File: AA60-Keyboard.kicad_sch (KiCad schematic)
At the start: 0 parts

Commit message: MCU/USB/Switch Matrix Schematics
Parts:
- added C1: 4.7uF, symbol Device:C
- added C2, C4, C5: 0.1uF, symbol Device:C
- added C3, C6, C7: 1uF, symbol Device:C
- added F1: 1A, symbol Device:Polyfuse
- added J2: USB_C_Receptacle_USB2.0_16P, symbol Connector:USB_C_Receptacle_USB2.0_16P
- added R1: 10k, symbol Device:R
- added R2, R3: 5.1k, symbol Device:R
- added SW1: SW_Push, symbol Switch:SW_Push
- added SW2: SW_SPDT, symbol Switch:SW_SPDT
- added U1: STM32G0B1CBTx, Package_QFP:LQFP-48_7x7mm_P0.5mm, symbol MCU_ST_STM32G0:STM32G0B1CBTx
- added U2: SRV05-4, Package_TO_SOT_SMD:SOT-23-6, symbol Power_Protection:SRV05-4
- added U3: XC6206P332MR, Package_TO_SOT_SMD:SOT-23-3, symbol Regulator_Linear:XC6206PxxxMR
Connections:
- new net: J2.B5 (CC2), R3.1
- new net: J2.A5 (CC1), R2.2
- new net: R1.1, SW2.2 (B)
- new net +3.3V: C1.1, C2.1, C3.1, C4.1, C7.1, SW2.3 (C), U1.4 (VBAT), U1.5 (VREF+), U1.6 (VDD), U3.2 (VO)
- new net +5V: C6.1, F1.2, U2.5 (VP), U3.3 (VI)
- new net BOOT0: R1.2, U1.36 (PA14)
- new net GND: C1.2, C2.2, C3.2, C4.2, C5.2, C6.2, C7.2, J2.A1 (GND), J2.A12 (GND), J2.B1 (GND), J2.B12 (GND), J2.S1 (SHIELD), R2.1, R3.2, SW1.2, SW2.1 (A), U1.7 (VSS), U2.2 (VN), U3.1 (GND)
- new net USB_DM: J2.A7 (D-), J2.B7 (D-), U1.33 (PA9/PA11)
- new net USB_DP: J2.A6 (D+), J2.B6 (D+), U1.34 (PA10/PA12)
- new net VBUS: F1.1, J2.A4 (VBUS), J2.A9 (VBUS), J2.B4 (VBUS), J2.B9 (VBUS)
- new net nRST: C5.1, SW1.1, U1.10 (PF2)
- no-connect marks 0 -> 2
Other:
- added sheet Switch Matrix (matrix.kicad_sch)

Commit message: Footprints
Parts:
- C1, C2, C3, C4, C5, C6, C7: footprint (none) -> Capacitor_SMD:C_0805_2012Metric
- F1: footprint (none) -> Fuse:Fuse_1206_3216Metric
- J2: footprint (none) -> Connector_USB:USB_C_Receptacle_HRO_TYPE-C-31-M-12
- R1, R2, R3: footprint (none) -> Resistor_SMD:R_0805_2012Metric
- SW1: footprint (none) -> Button_Switch_SMD:SW_SPST_TS-1088-xR020
- SW2: footprint (none) -> Button_Switch_SMD:SW_SPDT_PCM12
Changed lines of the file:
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@@
 			)
 		)
-		(property "Footprint" ""
+		(property "Footprint" "Capacitor_SMD:C_0805_2012Metric"
 			(at 139.3952 101.6 0)
 			(effects
@@
 			)
 		)
-		(property "Footprint" ""
+		(property "Footprint" "Resistor_SMD:R_0805_2012Metric"
 			(at 158.242 132.08 90)
 			(effects
@@
 			)
 		)
-		(property "Footprint" ""
+		(property "Footprint" "Resistor_SMD:R_0805_2012Metric"
 			(at 171.958 132.08 90)
 			(effects
@@
 			)
 		)
-		(property "Footprint" ""
+		(property "Footprint" "Capacitor_SMD:C_0805_2012Metric"
 			(at 36.5252 33.02 0)
 			(effects
@@
 			)
 		)
-		(property "Footprint" ""
+		(property "Footprint" "Capacitor_SMD:C_0805_2012Metric"
 			(at 110.1852 101.6 0)
 			(effects
@@
 			)
 		)
-		(property "Footprint" ""
+		(property "Footprint" "Capacitor_SMD:C_0805_2012Metric"
 			(at 23.8252 33.02 0)
 			(effects
@@
 			)
 		)
-		(property "Footprint" ""
+		(property "Footprint" "Capacitor_SMD:C_0805_2012Metric"
 			(at 23.8252 60.96 0)
 			(effects
@@
 			)
 		)
-		(property "Footprint" ""
+		(property "Footprint" "Resistor_SMD:R_0805_2012Metric"
 			(at 72.39 57.658 90)
 			(effects
@@
 			)
 		)
-		(property "Footprint" ""
+		(property "Footprint" "Button_Switch_SMD:SW_SPST_TS-1088-xR020"
 			(at 72.39 27.94 0)
 			(effects
@@
 			)
 		)
-		(property "Footprint" ""
+		(property "Footprint" "Connector_USB:USB_C_Receptacle_HRO_TYPE-C-31-M-12"
 			(at 120.65 135.89 0)
 			(effects
@@
 			)
 		)
-		(property "Footprint" ""
+		(property "Footprint" "Fuse:Fuse_1206_3216Metric"
 			(at 158.75 119.38 0)
 			(effects
@@
 			)
 		)
-		(property "Footprint" ""
+		(property "Footprint" "Button_Switch_SMD:SW_SPDT_PCM12"
 			(at 63.5 55.88 0)
 			(effects
@@
 			)
 		)
-		(property "Footprint" ""
+		(property "Footprint" "Capacitor_SMD:C_0805_2012Metric"
 			(at 36.5252 60.96 0)
 			(effects
@@
 			)
 		)
-		(property "Footprint" ""
+		(property "Footprint" "Capacitor_SMD:C_0805_2012Metric"
 			(at 56.8452 30.48 0)
 			(effects

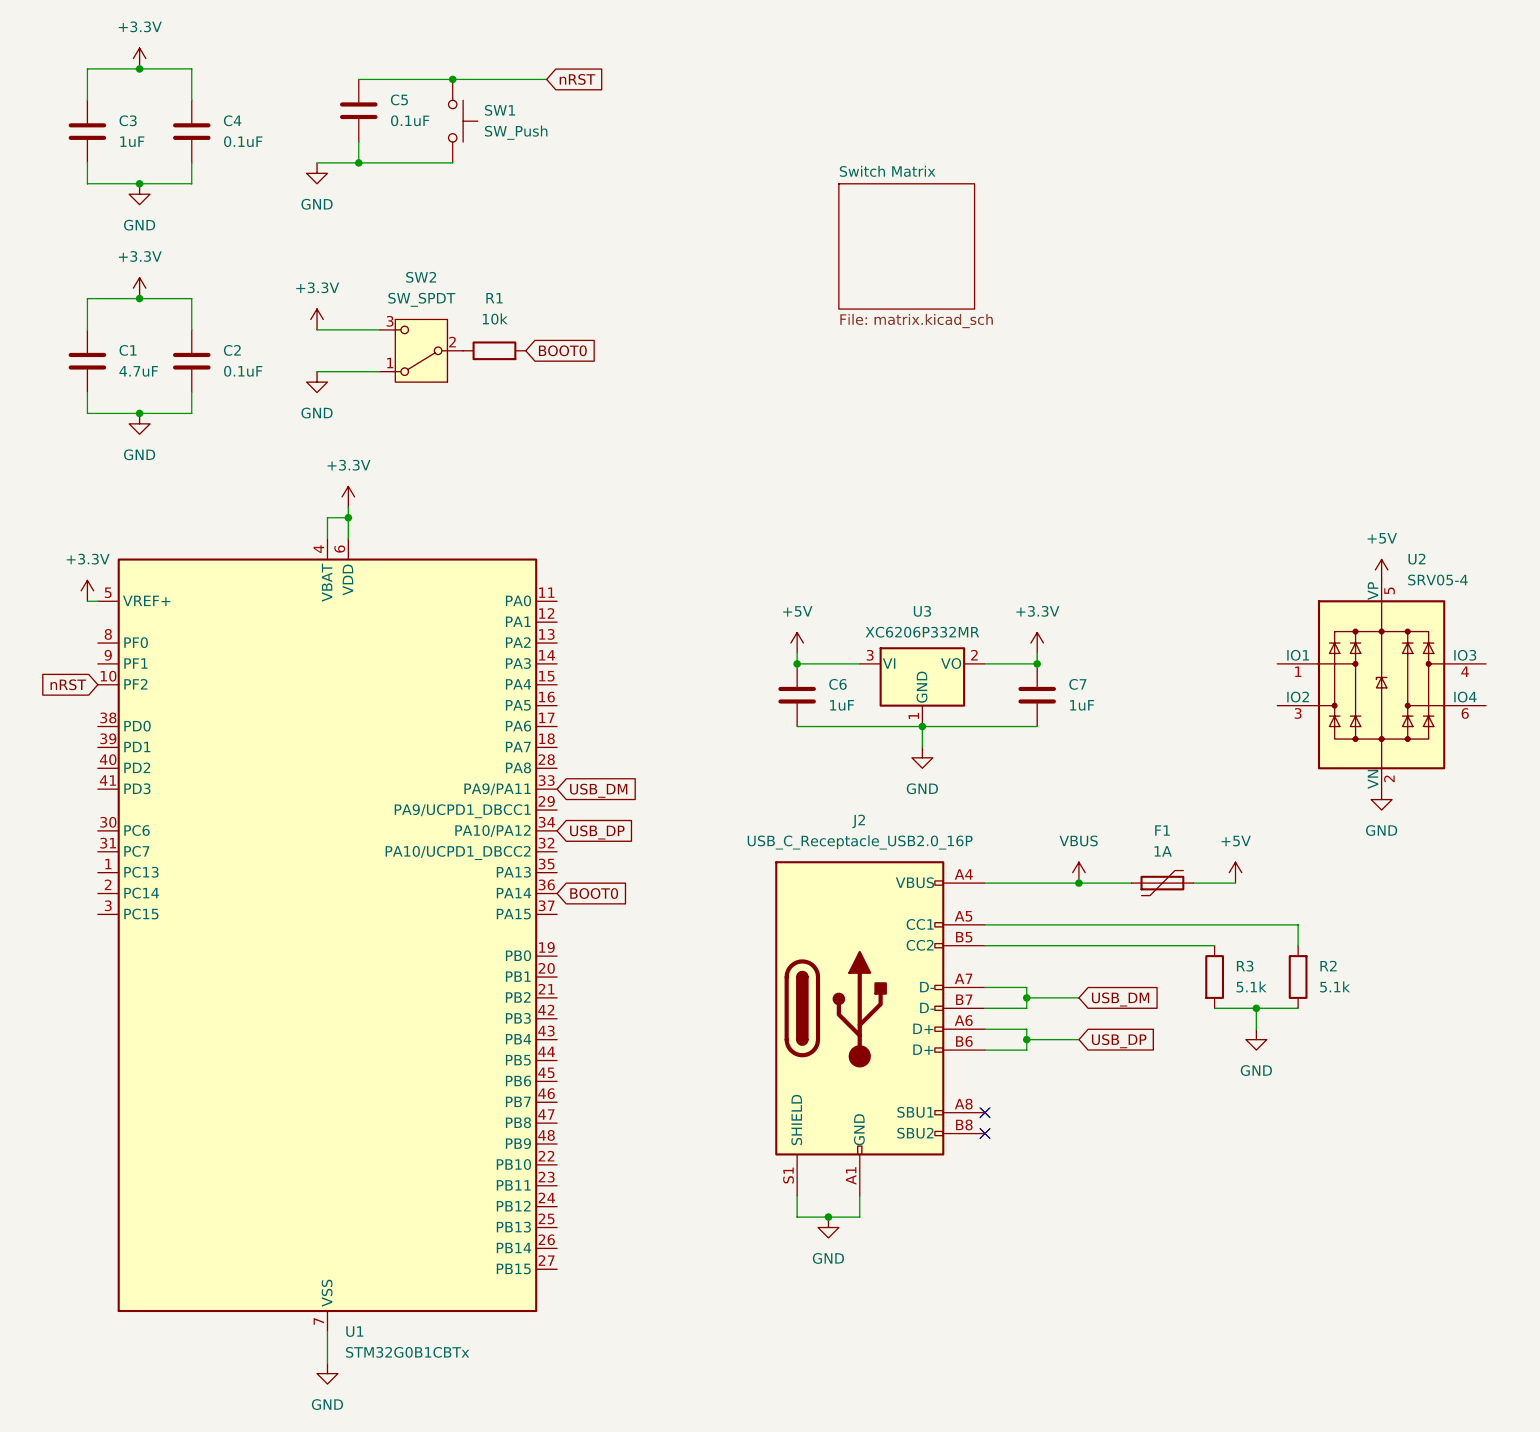
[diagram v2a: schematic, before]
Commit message: USB and microcontroller circuits wired (is ESD for CC lines needed??)
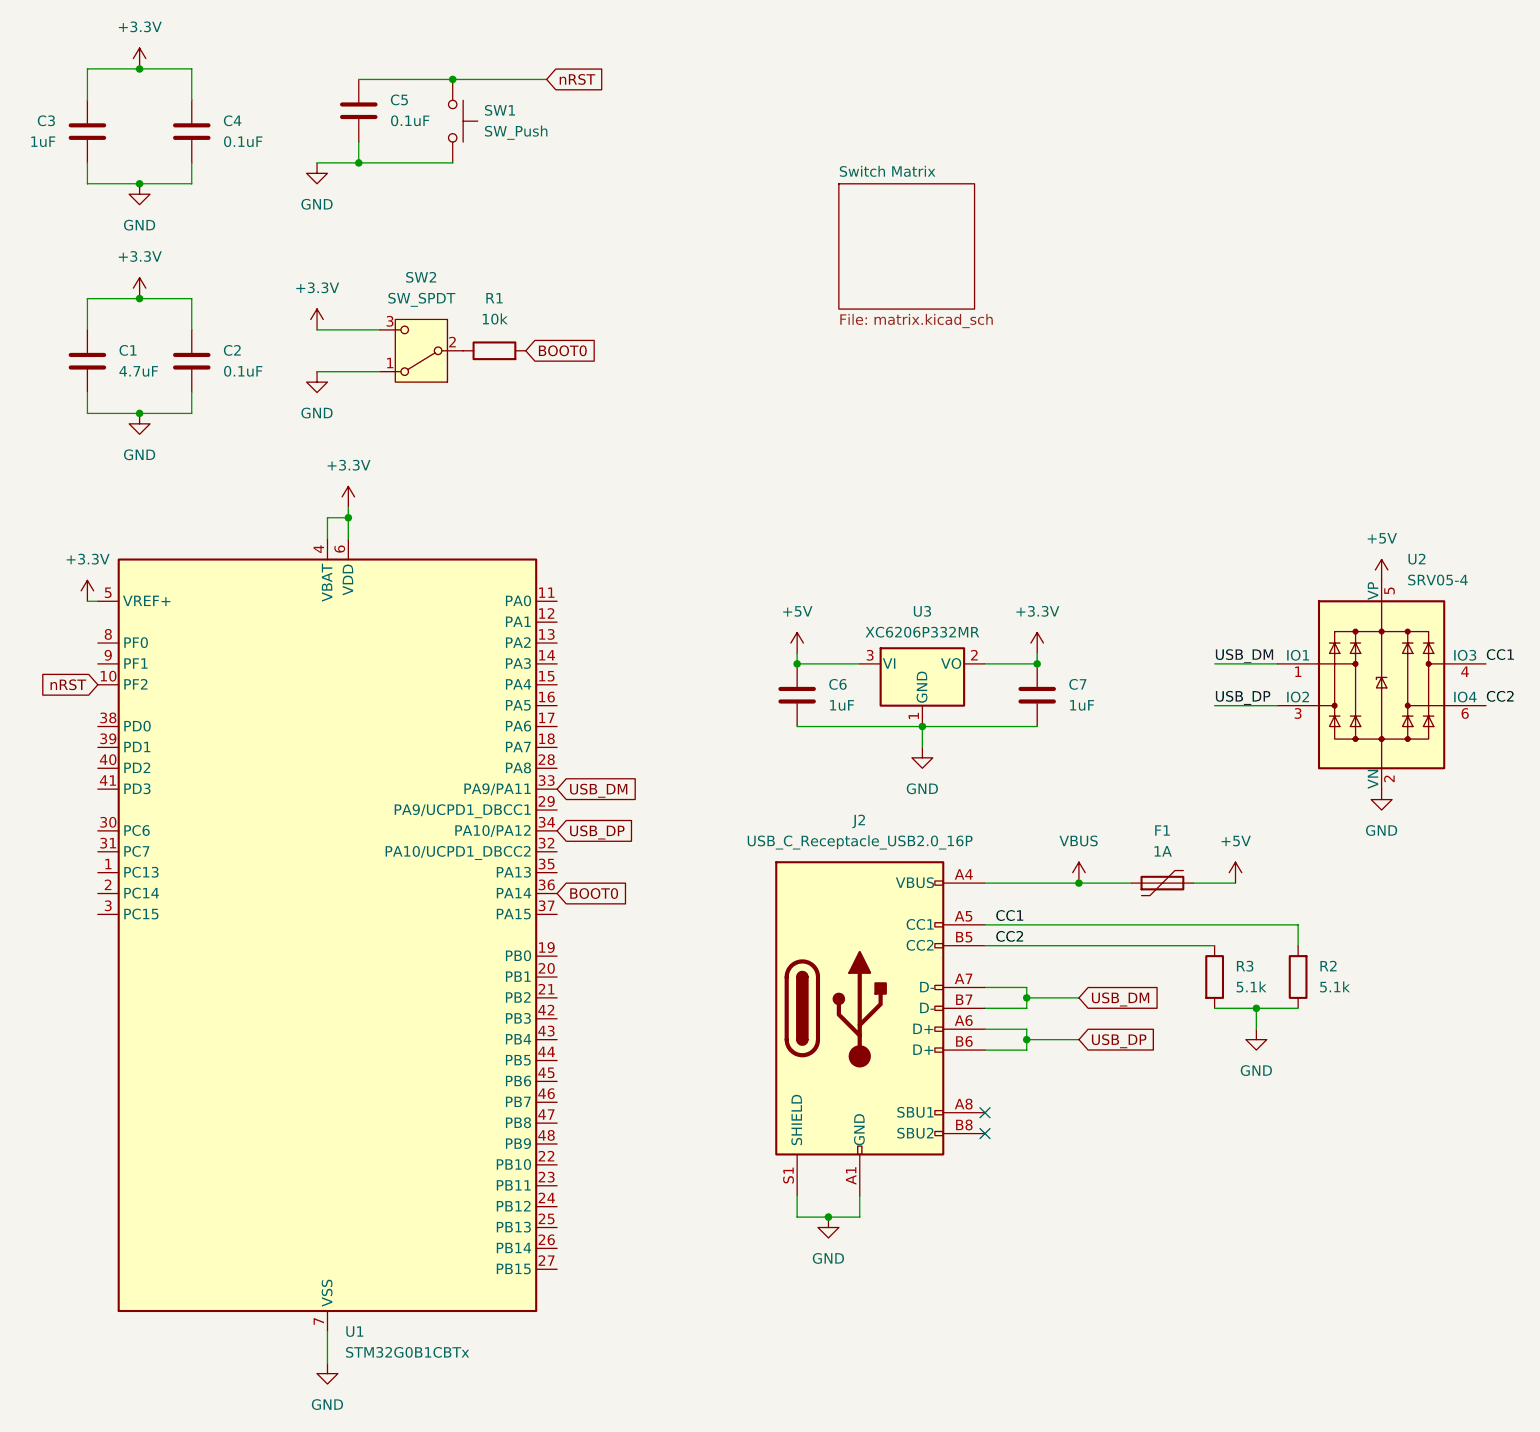
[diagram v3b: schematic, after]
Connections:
- net USB_DM: now also U2.1 (IO1)
- net USB_DP: now also U2.3 (IO2)
- net CC2: now reaches J2.B5 (CC2), R3.1
- net CC2: now also U2.6 (IO4)
- net CC1: now reaches J2.A5 (CC1), R2.2
- net CC1: now also U2.4 (IO3)
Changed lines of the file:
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@@
+	(wire
+		(pts
+			(xy 160.02 99.06) (xy 167.64 99.06)
+		)
+		(stroke
+			(width 0)
+			(type default)
+		)
+	)
 	(wire
 		(pts
@@
 	(wire
 		(pts
+			(xy 160.02 93.98) (xy 167.64 93.98)
+		)
+		(stroke
+			(width 0)
+			(type default)
+		)
+	)
+	(wire
+		(pts
 			(xy 35.56 35.56) (xy 35.56 33.02)
 		)
@@
 			(width 0)
 			(type default)
+		)
+	)
+	(label "CC1"
+		(at 193.04 93.98 0)
+		(effects
+			(font
+				(size 1.27 1.27)
+			)
+			(justify left bottom)
+		)
+	)
+	(label "CC1"
+		(at 133.35 125.73 0)
+		(effects
+			(font
+				(size 1.27 1.27)
+			)
+			(justify left bottom)
+		)
+	)
+	(label "USB_DP"
+		(at 160.02 99.06 0)
+		(effects
+			(font
+				(size 1.27 1.27)
+			)
+			(justify left bottom)
+		)
+	)
+	(label "USB_DM"
+		(at 160.02 93.98 0)
+		(effects
+			(font
+				(size 1.27 1.27)
+			)
+			(justify left bottom)
+		)
+	)
+	(label "CC2"
+		(at 193.04 99.06 0)
+		(effects
+			(font
+				(size 1.27 1.27)
+			)
+			(justify left bottom)
+		)
+	)
+	(label "CC2"
+		(at 133.35 128.27 0)
+		(effects
+			(font
+				(size 1.27 1.27)
+			)
+			(justify left bottom)
 		)
 	)
@@
 		(lib_id "Device:C")
 		(at 22.86 29.21 0)
+		(mirror y)
 		(unit 1)
 		(exclude_from_sim no)
@@
 		(dnp no)
 		(property "Reference" "C3"
-			(at 26.67 27.9399 0)
+			(at 19.05 27.9399 0)
 			(effects
 				(font
@@
 		)
 		(property "Value" "1uF"
-			(at 26.67 30.4799 0)
+			(at 19.05 30.4799 0)
 			(effects
 				(font
@@
 		)
 		(property "Footprint" "Capacitor_SMD:C_0805_2012Metric"
-			(at 23.8252 33.02 0)
-			(effects
-				(font
+			(at 21.8948 33.02 0)
+			(effects
+				(font

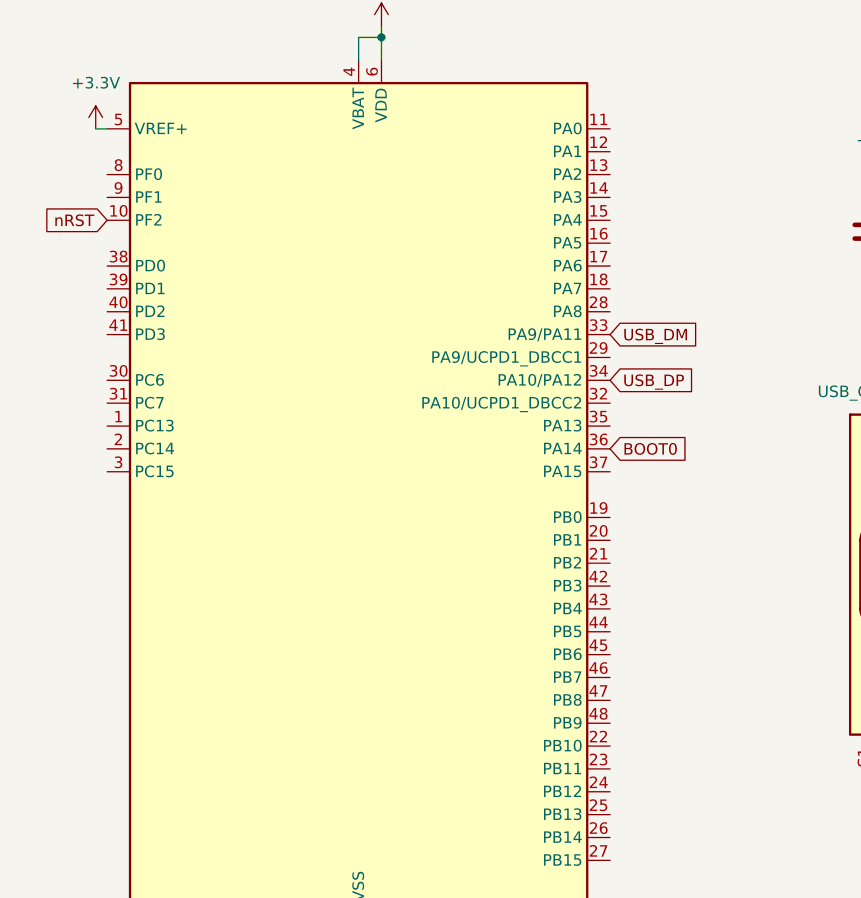
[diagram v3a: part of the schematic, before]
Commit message: Microcontroller Matrix Routed
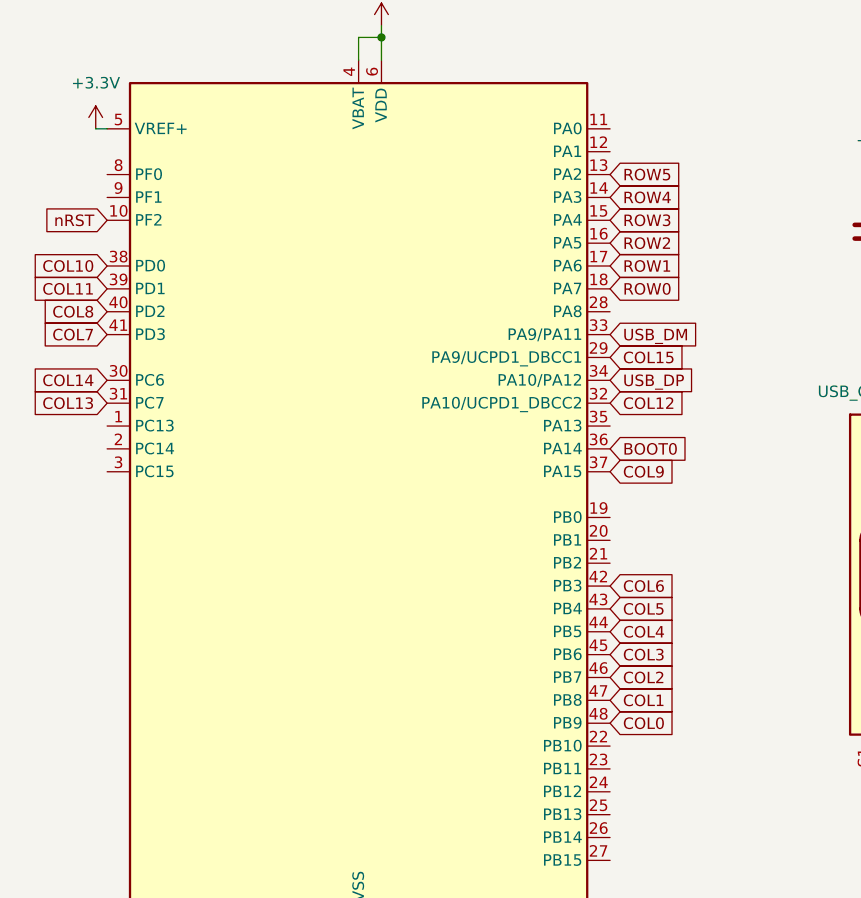
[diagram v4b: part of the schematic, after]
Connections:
- net ROW5: now reaches U1.13 (PA2)
- net ROW4: now reaches U1.14 (PA3)
- net ROW3: now reaches U1.15 (PA4)
- net ROW2: now reaches U1.16 (PA5)
- net ROW1: now reaches U1.17 (PA6)
- net ROW0: now reaches U1.18 (PA7)
- net COL15: now reaches U1.29 (PA9/UCPD1_DBCC1)
- net COL14: now reaches U1.30 (PC6)
- net COL13: now reaches U1.31 (PC7)
- net COL12: now reaches U1.32 (PA10/UCPD1_DBCC2)
- net COL9: now reaches U1.37 (PA15)
- net COL10: now reaches U1.38 (PD0)
- net COL11: now reaches U1.39 (PD1)
- net COL8: now reaches U1.40 (PD2)
- net COL7: now reaches U1.41 (PD3)
- net COL6: now reaches U1.42 (PB3)
- net COL5: now reaches U1.43 (PB4)
- net COL4: now reaches U1.44 (PB5)
- net COL3: now reaches U1.45 (PB6)
- net COL2: now reaches U1.46 (PB7)
- net COL1: now reaches U1.47 (PB8)
- net COL0: now reaches U1.48 (PB9)
